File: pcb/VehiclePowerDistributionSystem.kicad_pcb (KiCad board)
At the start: 4 copper layers, 70 x 70 mm, 85 parts, among them J1 B4B-XH-A, J2 B4B-XH-A, J3 B4B-XH-A, J4 B8B-XH-A, J5 B2B-XH-A, J6 FFC2B28-24-G, J7 B2B-XH-A, J8 B2B-XH-A, U1 TMC2209-LA-T, U2 TMC2209-LA-T, U3 TMC2209-LA-T, U4 D24V7F5, U5 D24V7F3, U8 BTS462TATMA1

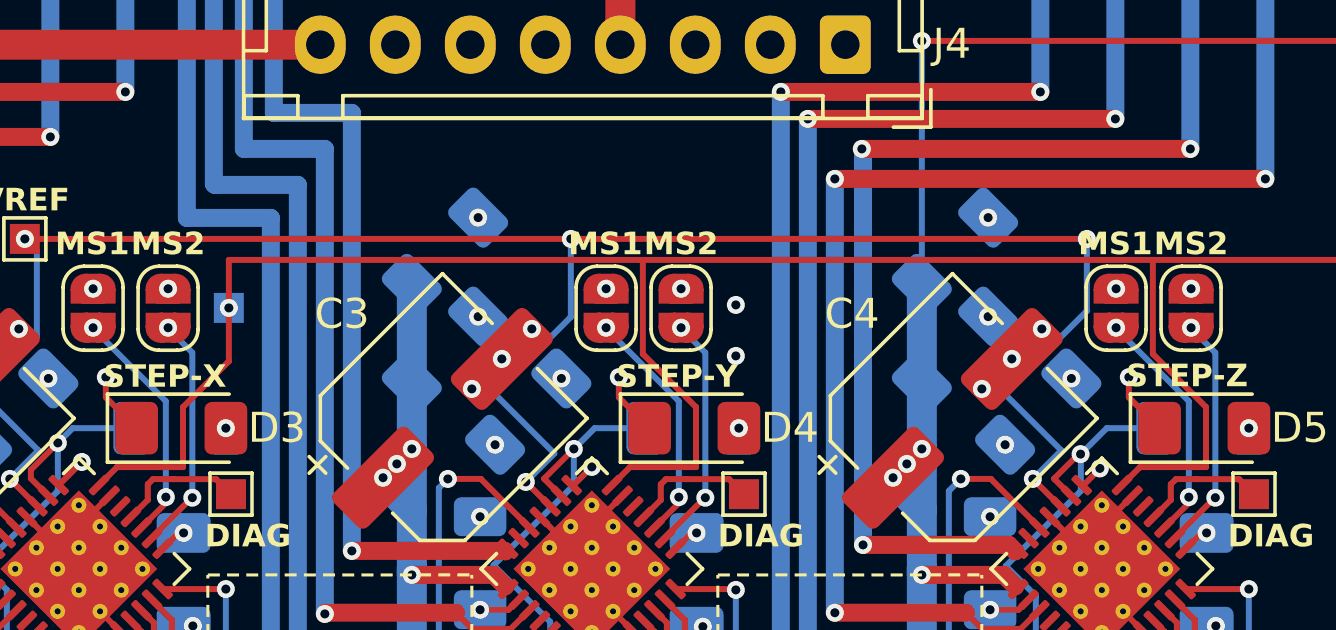
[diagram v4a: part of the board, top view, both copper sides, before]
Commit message: Moved test-pad for UART line of TMC2209s to top layer of `VehiclePowerDistributionSystem` PCB.
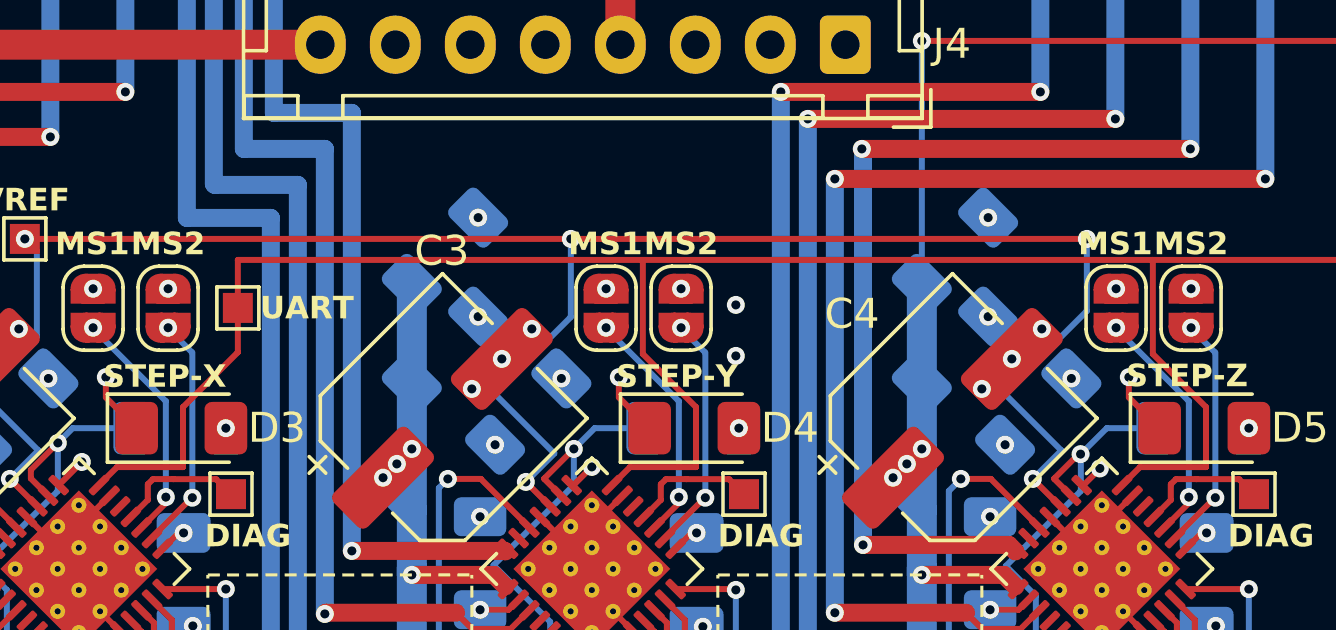
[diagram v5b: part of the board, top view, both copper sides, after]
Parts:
- TP5: moved to F.Cu
- moved TP5 0.30 mm to (138.5, 93.3)
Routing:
- net motor_uart_rx: track 139.0 -> 138.8 mm, vias 4 -> 3
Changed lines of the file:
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@@
 		(tags "capacitor electrolytic")
 		(property "Reference" "C3"
-			(at 0.094285 -4.827035 180)
+			(at 3.931371 -3.959798 180)
 			(layer "F.SilkS")
 			(effects
@@
 		(embedded_fonts no)
 	)
+	(footprint "TestPoint:TestPoint_Pad_1.0x1.0mm"
+		(layer "F.Cu")
+		(at 138.5 93.300001 -90)
+		(descr "SMD rectangular pad as test Point, square 1.0mm side length")
+		(tags "test point SMD pad rectangle square")
+		(property "Reference" "TP5"
+			(at 0 -1.448001 90)
+			(layer "F.SilkS")
+			(hide yes)
+			(effects
+				(font
+					(size 1 1)
+					(thickness 0.15)
+				)
+			)
+		)
+		(property "Value" "TestPoint"
+			(at 0 1.550001 90)
+			(layer "F.Fab")
+			(effects
+				(font
+					(size 1 1)
+					(thickness 0.15)
+				)
+			)
+		)
+		(property "Datasheet" "~"
+			(at 0 0 270)
+			(unlocked yes)
+			(layer "F.Fab")
+			(hide yes)
+			(effects
+				(font
+					(size 1.27 1.27)
+					(thickness 0.15)
+				)
+			)
+		)
+		(property "Description" "test point"
+			(at 0 0 270)
+			(unlocked yes)
+			(layer "F.Fab")
+			(hide yes)
+			(effects
+				(font
+					(size 1.27 1.27)
+					(thickness 0.15)
+				)
+			)
+		)
+		(property ki_fp_filters "Pin* Test*")
+		(sheetname "/")
+		(sheetfile "VehiclePowerDistributionSystem.kicad_sch")
+		(attr exclude_from_pos_files)
+		(fp_line
+			(start -0.7 0.7)
+			(end -0.7 -0.7)
+			(stroke
+				(width 0.12)
+				(type solid)
+			)
+			(layer "F.SilkS")
+		)
+		(fp_line
+			(start 0.7 0.7)
+			(end -0.7 0.7)
+			(stroke
+				(width 0.12)
+				(type solid)
+			)
+			(layer "F.SilkS")
+		)
+		(fp_line
+			(start -0.7 -0.7)
+			(end 0.7 -0.7)
+			(stroke
+				(width 0.12)
+				(type solid)
+			)
+			(layer "F.SilkS")
+		)
+		(fp_line
+			(start 0.7 -0.7)
+			(end 0.7 0.7)
+			(stroke
+				(width 0.12)
+				(type solid)
+			)
+			(layer "F.SilkS")
+		)
+		(fp_line
+			(start 1 1)
+			(end -1 1)
+			(stroke
+				(width 0.05)
+				(type solid)
+			)
+			(layer "F.CrtYd")
+		)
+		(fp_line
+			(start 1 1)
+			(end 1 -1)
+			(stroke
+				(width 0.05)
+				(type solid)
+			)
+			(layer "F.CrtYd")
+		)
+		(fp_line
+			(start -1 -1)
+			(end -1 1)
+			(stroke
+				(width 0.05)
+				(type solid)
+			)
+			(layer "F.CrtYd")
+		)
+		(fp_line
+			(start -1 -1)
+			(end 1 -1)
+			(stroke
+				(width 0.05)
+				(type solid)
+			)
+			(layer "F.CrtYd")
+		)
+		(fp_text user "${REFERENCE}"
+			(at 0 -1.45 90)
+			(layer "F.Fab")
+			(effects
+				(font
+					(size 1 1)
+					(thickness 0.15)
+				)
+			)
+		)
+		(pad "1" smd rect
+			(at 0 0 270)
+			(size 1 1)
+			(layers "F.Cu" "F.Mask")
+			(net 47 "motor_uart_rx")
+			(pinfunction "1")
+			(pintype "passive")
+		)
+		(embedded_fonts no)
+	)
 	(footprint "Connector_JST:JST_XH_B8B-XH-A_1x08_P2.50mm_Vertical"
 		(locked yes)
@@
 		)
 	)
-	(footprint "TestPoint:TestPoint_Pad_1.0x1.0mm"
-		(layer "B.Cu")
-		(at 138.2 93.300001 -90)
-		(descr "SMD rectangular pad as test Point, square 1.0mm side length")
-		(tags "test point SMD pad rectangle square")
-		(property "Reference" "TP5"
-			(at 0 1.448001 90)
-			(layer "B.SilkS")
-			(hide yes)
-			(effects
-				(font
-					(size 1 1)
-					(thickness 0.15)
-				)
-				(justify mirror)
-			)
-		)
-		(property "Value" "TestPoint"
-			(at 0 -1.550001 90)
-			(layer "B.Fab")
-			(effects
-				(font
-					(size 1 1)
-					(thickness 0.15)
-				)
-				(justify mirror)
-			)
-		)
-		(property "Datasheet" "~"
-			(at 0 0 90)
-			(unlocked yes)
-			(layer "B.Fab")
-			(hide yes)
-			(effects
-				(font
-					(size 1.27 1.27)
-					(thickness 0.15)
-				)
-				(justify mirror)
-			)
-		)
-		(property "Description" "test point"
-			(at 0 0 90)
-			(unlocked yes)
-			(layer "B.Fab")
-			(hide yes)
-			(effects
-				(font
-					(size 1.27 1.27)
-					(thickness 0.15)
-				)
-				(justify mirror)
-			)
-		)
-		(property ki_fp_filters "Pin* Test*")
-		(sheetname "/")
-		(sheetfile "VehiclePowerDistributionSystem.kicad_sch")
-		(attr exclude_from_pos_files)
-		(fp_line
-			(start -0.7 0.7)
-			(end 0.7 0.7)
-			(stroke
-				(width 0.12)
-				(type solid)
-			)
-			(layer "B.SilkS")
-		)
-		(fp_line
-			(start 0.7 0.7)
-			(end 0.7 -0.7)
-			(stroke
-				(width 0.12)
-				(type solid)
-			)
-			(layer "B.SilkS")
-		)
-		(fp_line
-			(start -0.7 -0.7)
-			(end -0.7 0.7)
-			(stroke
-				(width 0.12)
-				(type solid)
-			)
-			(layer "B.SilkS")
-		)
-		(fp_line
-			(start 0.7 -0.7)
-			(end -0.7 -0.7)
-			(stroke
-				(width 0.12)
-				(type solid)
-			)
-			(layer "B.SilkS")
-		)
-		(fp_line
-			(start -1 1)
-			(end 1 1)
-			(stroke
-				(width 0.05)
-				(type solid)
-			)
-			(layer "B.CrtYd")
-		)
-		(fp_line
-			(start -1 1)
-			(end -1 -1)
-			(stroke
-				(width 0.05)
-				(type solid)
-			)
-			(layer "B.CrtYd")
-		)
-		(fp_line
-			(start 1 -1)
-			(end 1 1)
-			(stroke
-				(width 0.05)
-				(type solid)
-			)
-			(layer "B.CrtYd")
-		)
-		(fp_line
-			(start 1 -1)
-			(end -1 -1)
-			(stroke
-				(width 0.05)
-				(type solid)
-			)
-			(layer "B.CrtYd")
-		)
-		(fp_text user "${REFERENCE}"
-			(at 0 1.45 90)
-			(layer "B.Fab")
-			(effects
-				(font
-					(size 1 1)
-					(thickness 0.15)
-				)
-				(justify mirror)
-			)
-		)
-		(pad "1" smd rect
-			(at 0 0 270)
-			(size 1 1)
-			(layers "B.Cu" "B.Mask")
-			(net 47 "motor_uart_rx")
-			(pinfunction "1")
-			(pintype "passive")
-		)
-		(embedded_fonts no)
-	)
 	(footprint "pcb:Flat Flexible Cable 24-Pin 0.5mm Connector"
 		(layer "B.Cu")
@@
 		)
 	)
+	(gr_text "UART"
+		(at 140.8 93.3 -0)
+		(layer "F.SilkS" knockout)
+		(effects
+			(font
+				(size 0.75 0.75)
+				(thickness 0.15)
+				(bold yes)
+			)
+		)
+	)
 	(gr_text "VPDS-R1"
 		(at 178.267993 126.019816 0)
@@
 		)
 	)
-	(gr_text "UART"
-		(at 138.2 92 0)
-		(layer "B.SilkS" knockout)
-		(effects
-			(font
-				(size 0.75 0.75)
-				(thickness 0.15)
-				(bold yes)
-			)
-			(justify mirror)
-		)
-	)
 	(segment
 		(start 151.678859 104.085965)
@@
 	)
 	(segment
-		(start 138.2 95.078677)
+		(start 138.5 94.778677)
 		(end 136.67175 96.606927)
 		(width 0.2)
@@
 	)
 	(segment
+		(start 134.472753 98.605928)
+		(end 133.871752 99.20693)
+		(width 0.2)
+		(layer "F.Cu")
+		(net 47)
+	)
+	(segment
 		(start 170.77175 98.605929)
 		(end 170.77175 96.606928)
@@
 	)
 	(segment
+		(start 138.5 91.7)
+		(end 169 91.7)
+		(width 0.2)
+		(layer "F.Cu")
+		(net 47)
+	)
+	(segment
 		(start 151.572754 98.605928)
 		(end 153.771751 98.605928)
@@
 	)
 	(segment
-		(start 138.2 91.7)
-		(end 138.2 93.300001)
+		(start 167.971752 99.20693)
+		(end 168.572754 98.605929)
 		(width 0.2)
 		(layer "F.Cu")
@@
 	)
 	(segment
-		(start 167.971752 99.20693)
-		(end 168.572754 98.605929)
+		(start 138.5 93.300001)
+		(end 138.5 94.778677)
+		(width 0.2)
+		(layer "F.Cu")
+		(net 47)
+	)
+	(segment
+		(start 136.67175 98.605928)
+		(end 134.472753 98.605928)
 		(width 0.2)
 		(layer "F.Cu")
@@
 	)
 	(segment
-		(start 138.2 93.300001)
-		(end 138.2 95.078677)
-		(width 0.2)
-		(layer "F.Cu")
-		(net 47)
-	)
-	(segment
 		(start 169 94.835178)
 		(end 169 91.7)
@@
 	)
 	(segment
-		(start 134.472753 98.605928)
-		(end 133.871752 99.20693)
-		(width 0.2)
-		(layer "F.Cu")
-		(net 47)
-	)
-	(segment
 		(start 153.771751 96.606927)
 		(end 152 94.835175)
@@
 	)
 	(segment
-		(start 136.67175 96.606927)
-		(end 136.67175 98.605928)
-		(width 0.2)
-		(layer "F.Cu")
-		(net 47)
-	)
-	(segment
-		(start 136.67175 98.605928)
-		(end 134.472753 98.605928)
+		(start 138.5 93.300001)
+		(end 138.5 91.7)
 		(width 0.2)
 		(layer "F.Cu")
@@
 	)
 	(segment
-		(start 169 91.7)
-		(end 138.2 91.7)
+		(start 136.67175 96.606927)
+		(end 136.67175 98.605928)
 		(width 0.2)
 		(layer "F.Cu")
 		(net 47)
 	)
-	(via
-		(at 138.2 93.300001)
-		(size 0.6)
-		(drill 0.3)
-		(layers "F.Cu" "B.Cu")
-		(net 47)
-	)

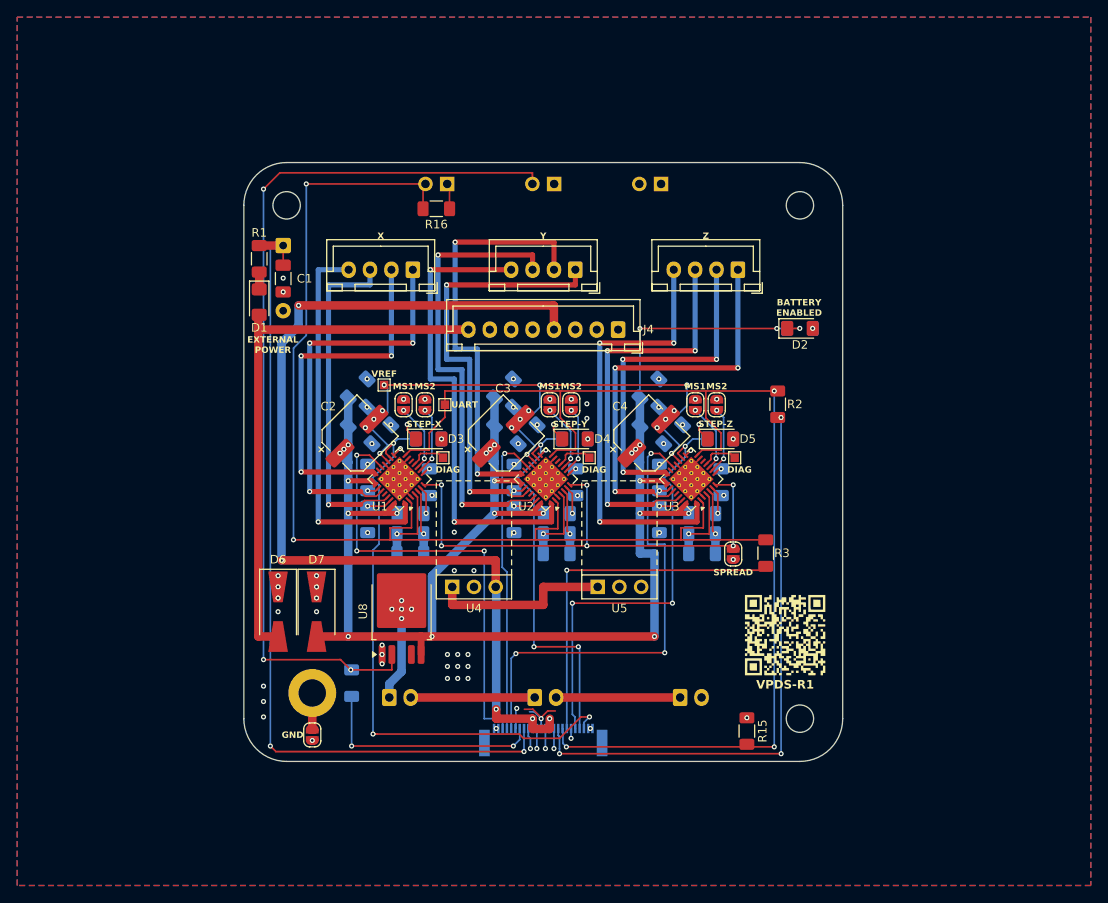
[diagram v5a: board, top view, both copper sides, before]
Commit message: Revised `VehiclePowerDistributionSystem`.
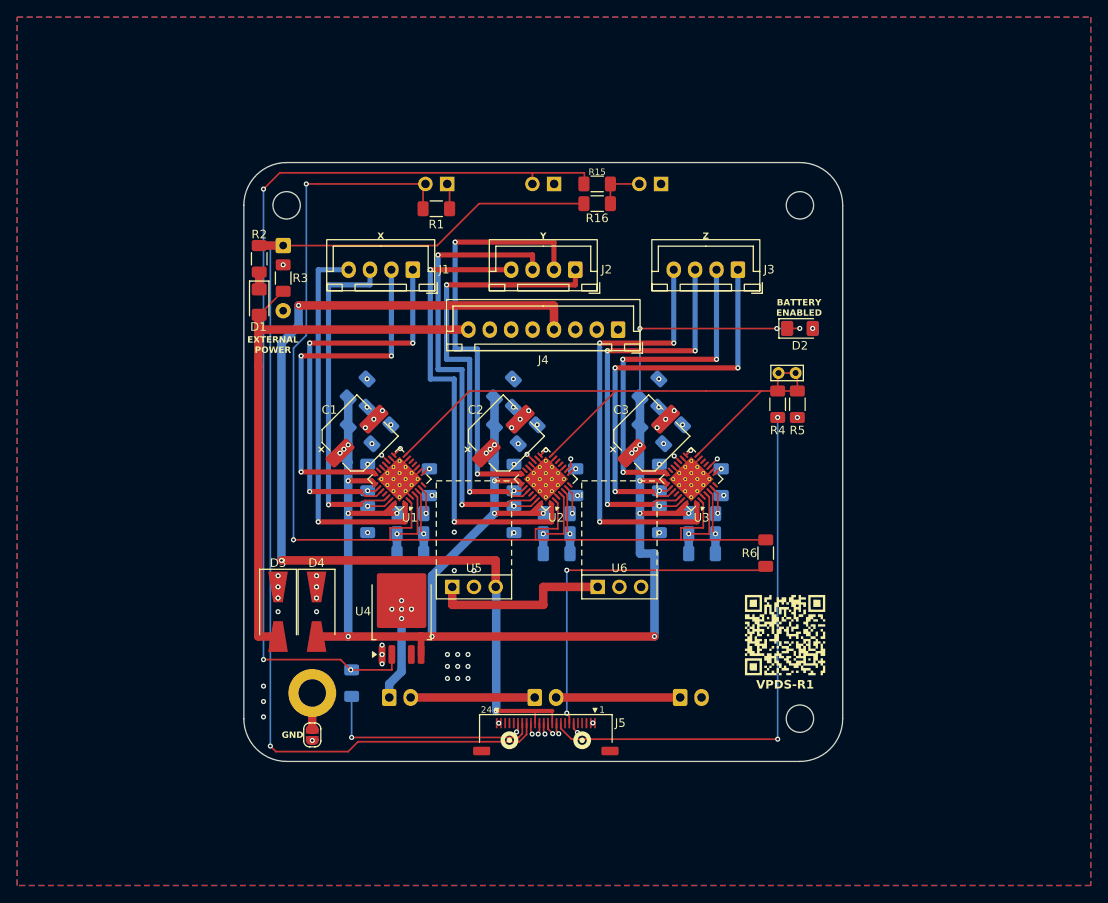
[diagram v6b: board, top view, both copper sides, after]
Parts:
- removed the C1 at (119.6, 78.6)
- removed the D3 at (136.6, 97.3)
- removed the D4 at (153.7, 97.3)
- removed the D5 at (170.7, 97.3)
- removed the J6 at (150.0, 132.5)
- removed JP1, JP2, JP3, JP4, JP5, JP6, JP7: SolderJumper_2_Open, Jumper:SolderJumper-2_P1.3mm_Open_RoundedPad1.0x1.5mm
- removed the R5 at (170.6, 97.3)
- removed the R6 at (153.7, 97.3)
- removed the R7 at (136.5, 97.3)
- removed TP1, TP3, TP4, TP5: TestPoint, TestPoint:TestPoint_Pad_1.0x1.0mm
- added J5: XF3M_2415_1B, pcb:XF3M_2415_1B - REVERSED, F.Cu at (156.1, 130.5)
- added R15: 100, Resistor_SMD:R_1206_3216Metric_Pad1.30x1.75mm_HandSolder, F.Cu at (156.3, 67.5)
- added R16: 1k, Resistor_SMD:R_1206_3216Metric_Pad1.30x1.75mm_HandSolder, F.Cu at (156.3, 69.8)
- added R3: 100k, Resistor_SMD:R_1206_3216Metric_Pad1.30x1.75mm_HandSolder, F.Cu at (119.6, 78.5)
- D3: renamed from D6; value SK34A -> SS24
- D4: renamed from D7; value SK34A -> SS24
- TP2: footprint TestPoint:TestPoint_Pad_1.0x1.0mm -> TestPoint:TestPoint_Bridge_Pitch2.0mm_Drill0.7mm
- moved TP2 42.4 mm to (179.5, 89.6), turned to 180 degrees
- moved R5 38.7 mm to (179.7, 93.2), turned to 90 degrees
- renumbered C2 to C1, C11 to C10, C12 to C11, C13 to C12, C14 to C13, C15 to C14, C16 to C15, C17 to C16, C18 to C17, C19 to C18, C21 to C19, C3 to C2, C22 to C21, C23 to C22, C24 to C23, C25 to C24, C4 to C3, C5 to C4, C6 to C5, C7 to C6, C8 to C7, C9 to C8, C10 to C9, D8 to D5, J5 to J6, R16 to R1, R1 to R2, R2 to R4, R15 to R5, R3 to R6, R4 to R7, U8 to U4, U4 to U5, U5 to U6
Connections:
- net /Stepper Motor Driver - X/DISABLE renamed /Stepper Motor Driver - X/ENABLE
- JP9 pad 1: unconnected-(JP9-A-Pad1) -> +3.3V
- JP9 pad 2: unconnected-(JP9-B-Pad2) -> BATTERY_AS_EXTERNAL
- R4 pad 1: motor_uart_tx -> motor_uart
- R4 pad 2: motor_uart_rx -> /Stepper Motor Driver - X/UART
- R5 pad 2: motor_uart_rx -> /Stepper Motor Driver - X/UART
- R6 pad 1: motor_disable -> motor_enable
- TP2 pad 1: Net-(U1-DIAG) -> /Stepper Motor Driver - X/UART
- U1 pad 10: Net-(JP2-B) -> GND
- U1 pad 11: Net-(U1-DIAG) -> unconnected-(U1-DIAG-Pad11)
- U1 pad 14: motor_uart_rx -> /Stepper Motor Driver - X/UART
- U1 pad 16: motor_step_x -> GND
- U1 pad 17: /Stepper Motor Driver - X/VREF -> +3.3V
- U1 pad 19: motor_direction_x -> GND
- U1 pad 7: /Stepper Motor Driver - X/SPREAD -> unconnected-(U1-SPREAD-Pad7)
- U1 pad 9: Net-(JP1-B) -> GND
- U2 pad 10: Net-(JP3-B) -> GND
- U2 pad 11: Net-(U2-DIAG) -> unconnected-(U2-DIAG-Pad11)
- U2 pad 14: motor_uart_rx -> /Stepper Motor Driver - X/UART
- U2 pad 16: motor_step_y -> GND
- U2 pad 17: /Stepper Motor Driver - X/VREF -> +3.3V
- U2 pad 19: motor_direction_y -> GND
- U2 pad 7: /Stepper Motor Driver - X/SPREAD -> unconnected-(U2-SPREAD-Pad7)
- U2 pad 9: Net-(JP4-B) -> +3.3V
- U3 pad 10: Net-(JP5-B) -> +3.3V
- U3 pad 11: Net-(U3-DIAG) -> unconnected-(U3-DIAG-Pad11)
- U3 pad 14: motor_uart_rx -> /Stepper Motor Driver - X/UART
- U3 pad 16: motor_step_z -> GND
- U3 pad 17: /Stepper Motor Driver - X/VREF -> +3.3V
- U3 pad 19: motor_direction_z -> GND
- U3 pad 7: /Stepper Motor Driver - X/SPREAD -> unconnected-(U3-SPREAD-Pad7)
- U3 pad 9: Net-(JP6-B) -> GND
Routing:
- net motor_uart_rx: track 138.8 -> 0.00 mm, vias 3 -> 0
- net /Stepper Motor Driver - X/UART: track 0.00 -> 76.1 mm
- net /Stepper Motor Driver - X/VREF: track 70.0 -> 0.00 mm, vias 6 -> 0
- net motor_step_x: track 68.9 -> 0.00 mm, vias 3 -> 0
- net motor_uart_tx: track 68.2 -> 0.00 mm, vias 3 -> 0
- net motor_uart: track 0.00 -> 64.1 mm, vias 0 -> 2
- net /Stepper Motor Driver - X/SPREAD: track 61.6 -> 0.00 mm, vias 6 -> 0
- net motor_direction_z: track 55.2 -> 0.00 mm, vias 3 -> 0
- net motor_direction_x: track 52.5 -> 0.00 mm, vias 3 -> 0
- net motor_step_z: track 51.2 -> 0.00 mm, vias 3 -> 0
- net motor_step_y: track 45.3 -> 0.00 mm, vias 3 -> 0
- net motor_disable: track 41.9 -> 0.00 mm, vias 1 -> 0
- net motor_enable: track 0.00 -> 41.4 mm, vias 0 -> 2
- net motor_direction_y: track 35.9 -> 0.00 mm, vias 1 -> 0
- net external_detected: track 97.7 -> 132.4 mm, vias 2 -> 1
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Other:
- board text added: "BATTERY AS EXTERNAL"
- board text removed: "DIAG"
- board text removed: "MS1"
- board text removed: "MS2"
- board text removed: "SPREAD"
- board text removed: "STEP-X"
- board text removed: "STEP-Y"
- board text removed: "STEP-Z"
- board text removed: "UART"
- board text removed: "UNUSED"
- board text removed: "VREF"
